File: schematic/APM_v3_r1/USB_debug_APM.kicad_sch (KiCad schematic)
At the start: 16 parts, among them J29 USB_A, J30 UART_DEBUG, U38 CH340G, Y7 12MHz

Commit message: APM v3?
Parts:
- J30: footprint Connector_PinHeader_2.54mm:PinHeader_1x03_P2.54mm_Horizontal -> Connector_PinHeader_2.54mm:PinHeader_1x03_P2.54mm_Vertical
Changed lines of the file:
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@@
 			)
 		)
-		(property "Footprint" "Connector_PinHeader_2.54mm:PinHeader_1x03_P2.54mm_Horizontal"
+		(property "Footprint" "Connector_PinHeader_2.54mm:PinHeader_1x03_P2.54mm_Vertical"
 			(at 177.8 115.57 0)
 			(effects

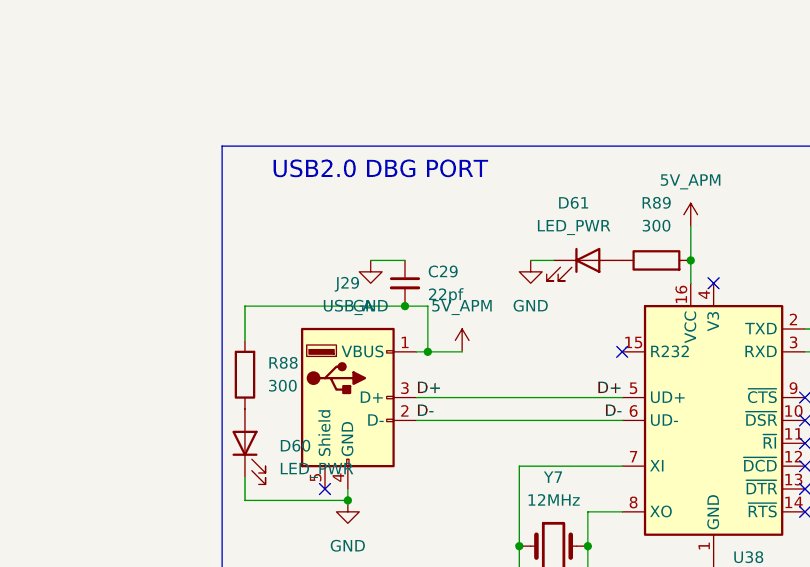
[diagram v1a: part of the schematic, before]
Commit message: updating top v10. need to get 3v3 APM converged in schematic. routing is tricky right now. the components should be evenly laid out and have the NUCLEO pins be adjusted based on location
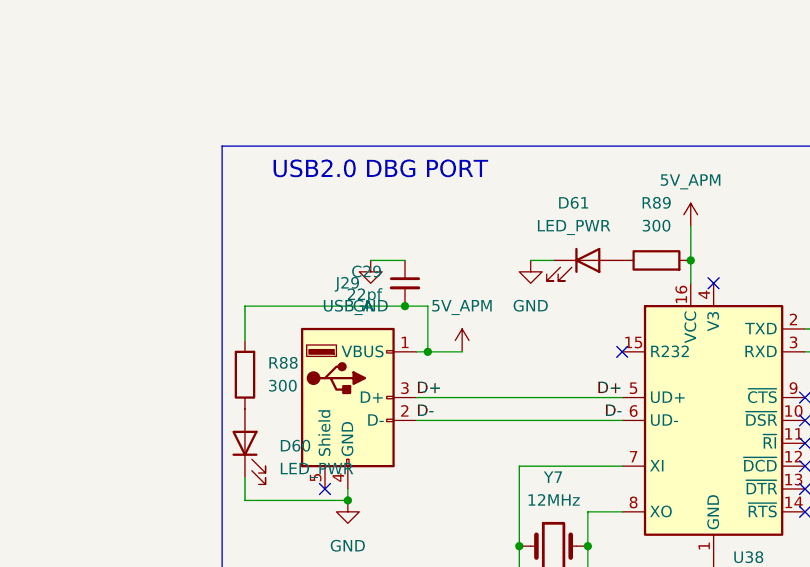
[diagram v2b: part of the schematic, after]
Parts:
- R88, R89, R90, R91, R92: footprint Resistor_SMD:R_0805_2012Metric_Pad1.20x1.40mm_HandSolder -> Resistor_SMD:R_0201_0603Metric

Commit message: i got orientation wrong big time
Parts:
- removed R90: 1k5, Resistor_SMD:R_0201_0603Metric, symbol Device:R
- R89: value 300 -> 1.2k
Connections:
- net APM_DBG_TX is gone; now on net USB_DBG_TX: J30.1 (Pin_1)
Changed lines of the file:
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@@
 	(wire
 		(pts
-			(xy 171.45 110.49) (xy 171.45 113.03)
+			(xy 124.46 68.58) (xy 124.46 73.66)
 		)
 		(stroke
@@
 	(wire
 		(pts
-			(xy 124.46 68.58) (xy 124.46 73.66)
+			(xy 168.91 115.57) (xy 172.72 115.57)
 		)
 		(stroke
@@
 	(wire
 		(pts
-			(xy 168.91 115.57) (xy 172.72 115.57)
+			(xy 171.45 99.06) (xy 182.88 99.06)
 		)
 		(stroke
@@
 	(wire
 		(pts
-			(xy 171.45 99.06) (xy 182.88 99.06)
+			(xy 104.14 68.58) (xy 104.14 72.39)
 		)
 		(stroke
@@
 	(wire
 		(pts
-			(xy 104.14 68.58) (xy 104.14 72.39)
+			(xy 153.67 59.69) (xy 153.67 63.5)
 		)
 		(stroke
@@
 	(wire
 		(pts
-			(xy 153.67 59.69) (xy 153.67 63.5)
+			(xy 124.46 73.66) (xy 128.27 73.66)
 		)
 		(stroke
@@
 	(wire
 		(pts
-			(xy 124.46 73.66) (xy 128.27 73.66)
+			(xy 124.46 73.66) (xy 123.19 73.66)
 		)
 		(stroke
@@
 	(wire
 		(pts
-			(xy 124.46 73.66) (xy 123.19 73.66)
+			(xy 168.91 83.82) (xy 171.45 83.82)
 		)
 		(stroke
@@
 	(wire
 		(pts
-			(xy 168.91 83.82) (xy 171.45 83.82)
+			(xy 168.91 101.6) (xy 168.91 115.57)
 		)
 		(stroke
@@
 	(wire
 		(pts
-			(xy 168.91 101.6) (xy 168.91 115.57)
+			(xy 134.62 86.36) (xy 134.62 95.25)
 		)
 		(stroke
@@
 	(wire
 		(pts
-			(xy 134.62 86.36) (xy 134.62 95.25)
+			(xy 123.19 81.28) (xy 146.05 81.28)
 		)
 		(stroke
@@
 	(wire
 		(pts
-			(xy 123.19 81.28) (xy 146.05 81.28)
+			(xy 104.14 90.17) (xy 104.14 87.63)
 		)
 		(stroke
@@
 	(wire
 		(pts
-			(xy 104.14 90.17) (xy 104.14 87.63)
+			(xy 135.89 63.5) (xy 138.43 63.5)
 		)
 		(stroke
@@
 	(wire
 		(pts
-			(xy 135.89 63.5) (xy 138.43 63.5)
+			(xy 171.45 71.12) (xy 171.45 99.06)
 		)
 		(stroke
@@
 	(wire
 		(pts
-			(xy 171.45 71.12) (xy 171.45 99.06)
+			(xy 104.14 68.58) (xy 121.92 68.58)
 		)
 		(stroke
@@
 	(wire
 		(pts
-			(xy 104.14 68.58) (xy 121.92 68.58)
+			(xy 153.67 63.5) (xy 153.67 66.04)
 		)
 		(stroke
@@
 	(wire
 		(pts
-			(xy 153.67 63.5) (xy 153.67 66.04)
+			(xy 121.92 68.58) (xy 124.46 68.58)
 		)
 		(stroke
@@
 	(wire
 		(pts
-			(xy 121.92 68.58) (xy 124.46 68.58)
-		)
-		(stroke
-			(width 0)
-			(type default)
-		)
-	)
-	(wire
-		(pts
-			(xy 171.45 99.06) (xy 171.45 102.87)
+			(xy 171.45 99.06) (xy 171.45 113.03)
 		)
 		(stroke
@@
 			)
 		)
-		(property "Value" "300"
+		(property "Value" "1.2k"
 			(at 149.86 59.69 90)
 			(show_name no)
@@
 					(unit 1)
 				)
-			)
-		)
-	)
-	(symbol
-		(lib_id "Device:R")
-		(at 171.45 106.68 180)
-		(unit 1)
-		(body_style 1)
-		(exclude_from_sim no)
-		(in_bom yes)
-		(on_board yes)
-		(in_pos_files yes)
-		(dnp no)
-		(fields_autoplaced yes)
-		(property "Reference" "R90"
-			(at 173.99 105.4099 0)
-			(show_name no)
-			(do_not_autoplace no)
-			(effects
-				(font
-					(size 1.27 1.27)
-				)
-				(justify right)
-			)
-		)
-		(property "Value" "1k5"
-			(at 173.99 107.9499 0)
-			(show_name no)
-			(do_not_autoplace no)
-			(effects
-				(font
-					(size 1.27 1.27)
-				)
-				(justify right)
-			)
-		)
-		(property "Footprint" "Resistor_SMD:R_0201_0603Metric"
-			(at 173.228 106.68 90)
-			(hide yes)
-			(show_name no)
-			(do_not_autoplace no)
-			(effects
-				(font
-					(size 1.27 1.27)
-				)
-			)
-		)
-		(property "Datasheet" ""
-			(at 171.45 106.68 0)
-			(hide yes)
-			(show_name no)
-			(do_not_autoplace no)
-			(effects
-				(font
-					(size 1.27 1.27)
-				)
-			)
-		)
-		(property "Description" "Resistor"
-			(at 171.45 106.68 0)
-			(hide yes)
-			(show_name no)
-			(do_not_autoplace no)
-			(effects
-				(font
-					(size 1.27 1.27)
-				)
-			)
-		)
-		(property "DigiKey_Part_Number" "311-10.0KCRCT-ND"
-			(at 171.45 106.68 0)
-			(hide yes)
-			(show_name no)
-			(do_not_autoplace no)
-			(effects
-				(font
-					(size 1.27 1.27)
-				)
-			)
-		)
-		(property "Price" "0.0129"
-			(at 171.45 106.68 0)
-			(hide yes)
-			(show_name no)
-			(do_not_autoplace no)
-			(effects
-				(font
-					(size 1.27 1.27)
-				)
-			)
-		)
-		(pin "2"
-		)
-		(pin "1"
-		)
-		(instances
-			(project "APM"
-				(path "/63e257c1-2fa4-4533-ab9e-932d24befb8c/fe366db2-c203-41e1-8153-079c5491bdc0"
-					(reference "R90")
-					(unit 1)
-				)
